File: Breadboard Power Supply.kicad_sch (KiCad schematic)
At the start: 33 parts, among them J1 USB-C Power Only, J10 Conn_01x02_Male, J11 Conn_01x02_Male, J12 217175-0001, J2 Conn_01x02_Male, J3 Conn_01x02_Male, J4 Conn_01x02_Male, J5 Conn_01x02_Male, J6 Conn_01x02_Male, J7 Conn_01x02_Male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

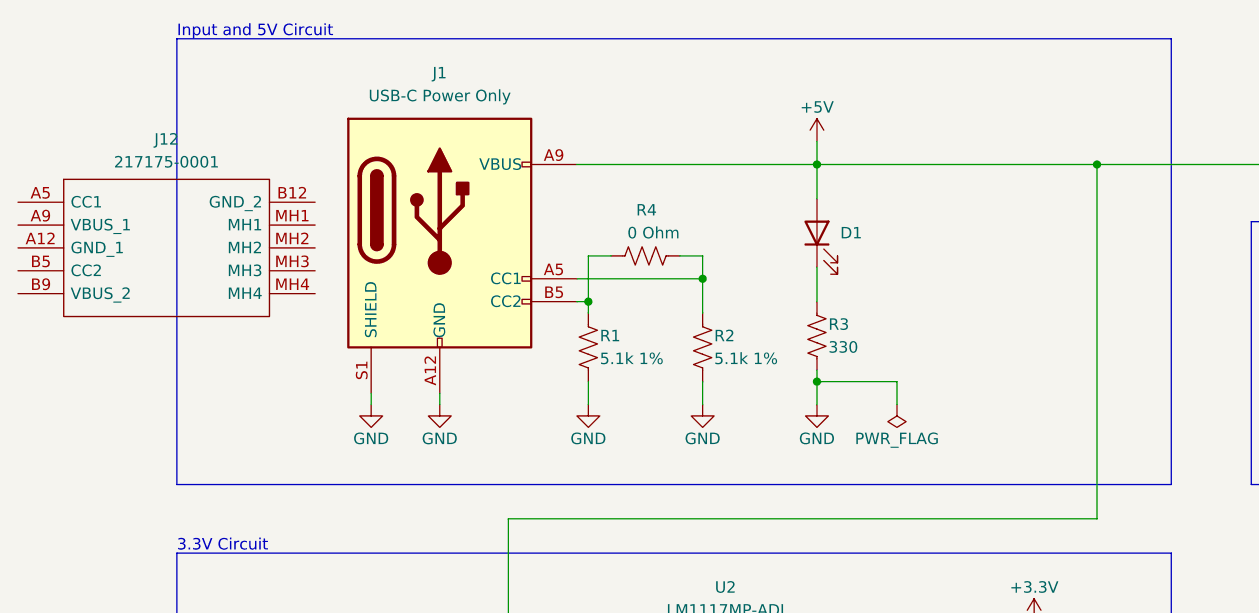
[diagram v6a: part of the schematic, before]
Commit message: Changed USB connector from through hole to surface mount.
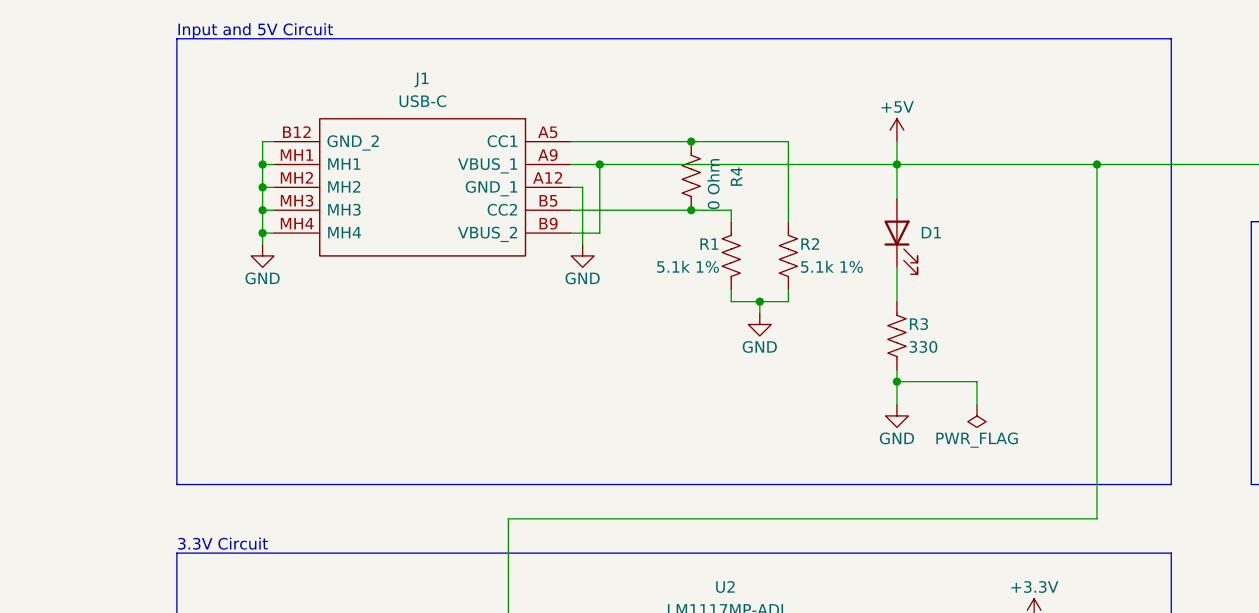
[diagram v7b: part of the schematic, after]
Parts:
- removed J1: USB-C Power Only, USC-C Surface Mount:2171750001, symbol Connector:USB_C_Receptacle_PowerOnly_6P
- J1: renamed from J12; value 217175-0001 -> USB-C
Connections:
- net +5V: now also J1.A9 (VBUS_1), J1.B9 (VBUS_2)
- net GND: now also J1.A12 (GND_1), J1.B12 (GND_2), J1.MH1, J1.MH2, J1.MH3, J1.MH4
- net at R4.1: now also J1.A5 (CC1), R2.1; no longer R1.1
- net at J1.B5 (CC2): now also R1.1, R4.2
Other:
- moved on the sheet: D1, J1, R3

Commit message: Updated some part numbers.
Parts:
- J1: Digi-Key Part Num (none) -> 900-2171750001CT-ND
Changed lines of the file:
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@@
       (effects (font (size 1.27 1.27)) (justify left) hide)
     )
-    (property "Datasheet" "https://www.molex.com/pdm_docs/sd/2171750001_sd.pdf" (at 59.055 41.91 0)
+    (property "Datasheet" "https://www.molex.com/webdocs/datasheets/pdf/en-us/2171750001_IO_CONNECTORS.pdf" (at 59.055 41.91 0)
       (effects (font (size 1.27 1.27)) (justify left) hide)
     )
@@
       (effects (font (size 1.27 1.27)) (justify left) hide)
     )
+    (property "Digi-Key Part Num" "900-2171750001CT-ND" (at 88.265 41.91 0)
+      (effects (font (size 1.27 1.27)) hide)
+    )
     (pin "A12")
